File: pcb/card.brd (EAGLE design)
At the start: 69.5 x 40.6 mm, 19 parts, among them IC1 74HC14D, IC2 24LC256SN, Q1 BC817

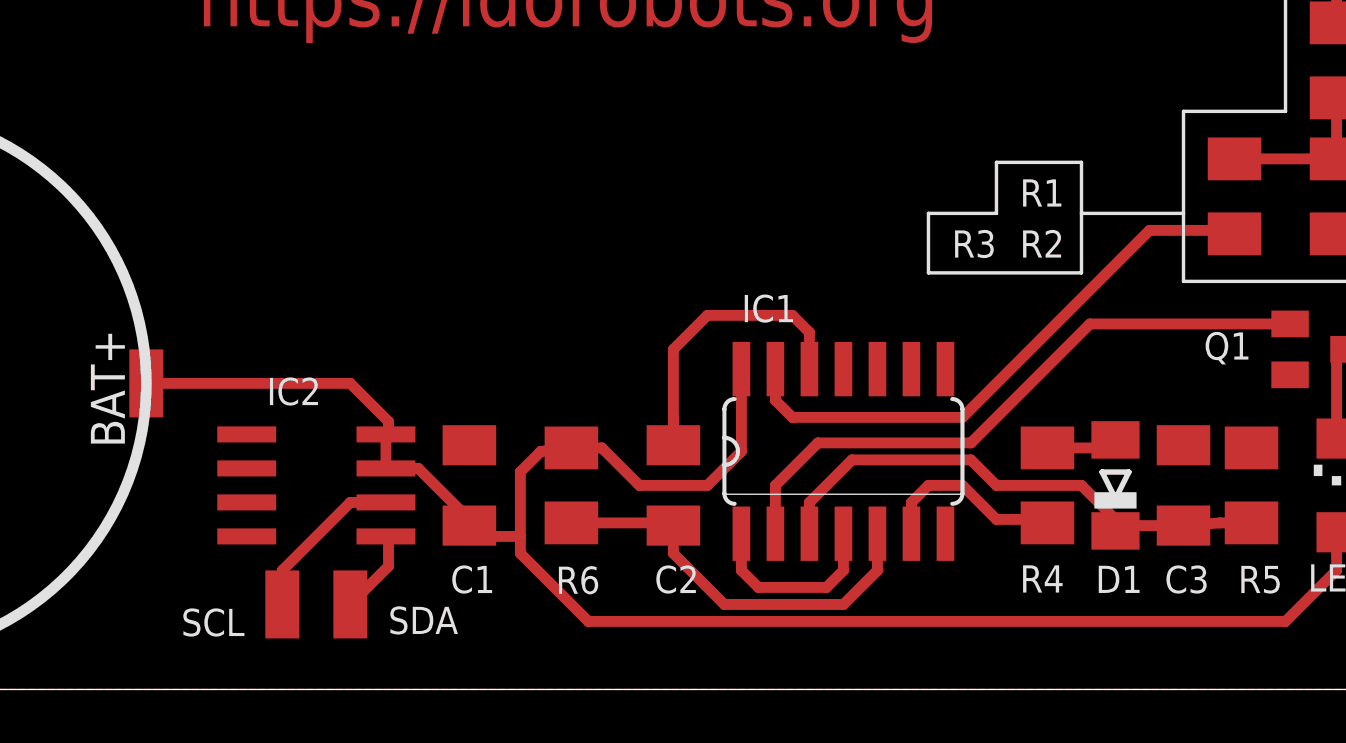
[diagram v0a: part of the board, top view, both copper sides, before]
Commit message: Added a GND pad for the EEPROM chip.
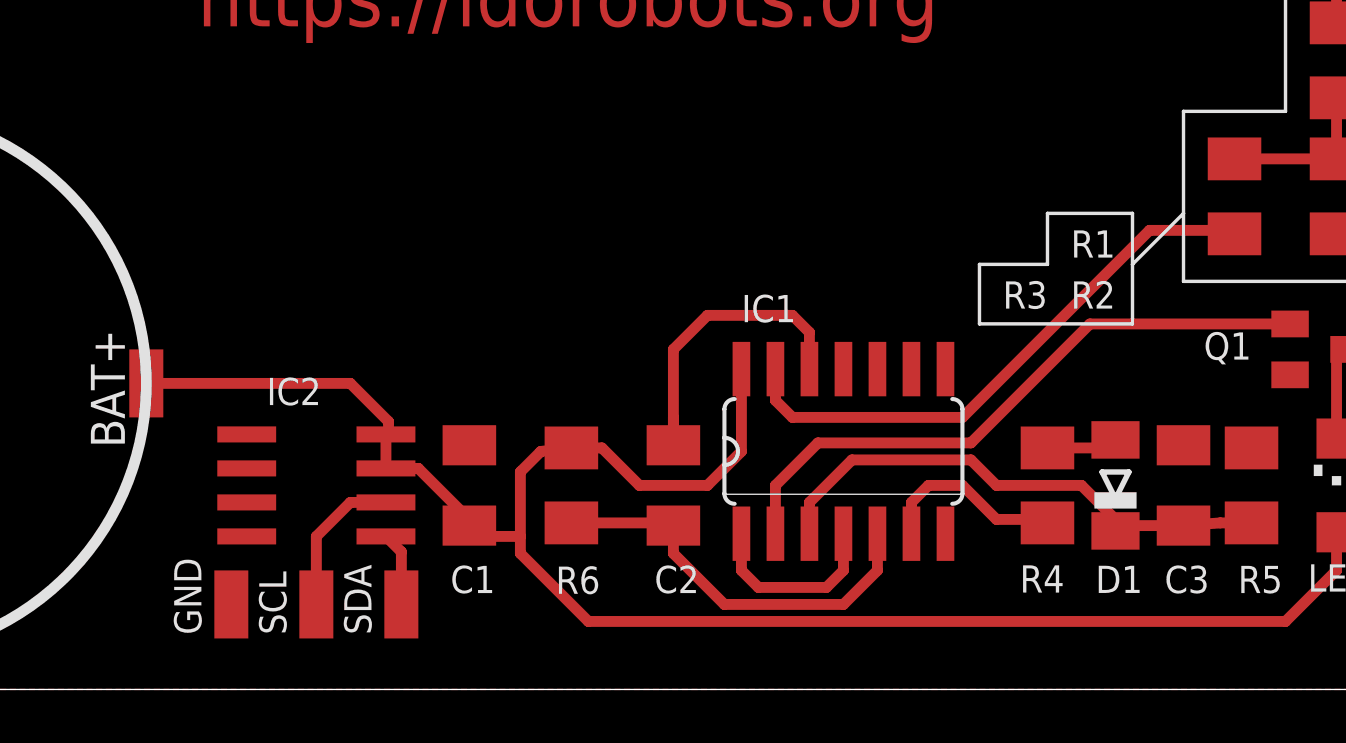
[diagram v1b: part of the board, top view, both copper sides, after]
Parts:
- added GND: (no value), wirepad:SMD1,27-2,54
- moved SDA 1.90 mm to (31.1, 3.17)
- moved SCL 1.27 mm to (27.9, 3.17)
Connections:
- net GND: now also GND.1
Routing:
- net N$9: track 6.19 -> 5.67 mm
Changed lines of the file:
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@@
 <setting verticaltext="up"/>
 </settings>
-<grid distance="0.635" unitdist="mm" unit="mm" style="lines" multiple="1" display="no" altdistance="0.003125" altunitdist="mic" altunit="mm"/>
+<grid distance="0.635" unitdist="mm" unit="mm" style="lines" multiple="1" display="no" altdistance="0.3175" altunitdist="mm" altunit="mm"/>
 <layers>
 <layer number="1" name="Top" color="4" fill="1" visible="yes" active="yes"/>
@@
 <text x="8.89" y="30.48" size="3.81" layer="29">Kajetan Rzepecki</text>
 <text x="23.495" y="24.765" size="2.1844" layer="29">https://idorobots.org</text>
-<wire x1="50.8" y1="15.5575" x2="56.515" y2="15.5575" width="0.127" layer="25"/>
-<wire x1="56.515" y1="15.5575" x2="56.515" y2="17.78" width="0.127" layer="25"/>
-<wire x1="56.515" y1="17.78" x2="56.515" y2="19.685" width="0.127" layer="25"/>
+<wire x1="52.705" y1="13.6525" x2="58.42" y2="13.6525" width="0.127" layer="25"/>
+<wire x1="58.42" y1="13.6525" x2="58.42" y2="15.875" width="0.127" layer="25"/>
+<wire x1="58.42" y1="15.875" x2="58.42" y2="17.78" width="0.127" layer="25"/>
 <wire x1="60.325" y1="15.24" x2="67.945" y2="15.24" width="0.127" layer="25"/>
 <wire x1="67.945" y1="15.24" x2="67.945" y2="26.67" width="0.127" layer="25"/>
 <wire x1="60.325" y1="17.78" x2="60.325" y2="15.24" width="0.127" layer="25"/>
-<wire x1="56.515" y1="17.78" x2="60.325" y2="17.78" width="0.127" layer="25"/>
-<wire x1="50.8" y1="15.5575" x2="50.8" y2="17.78" width="0.127" layer="25"/>
-<wire x1="50.8" y1="17.78" x2="53.34" y2="17.78" width="0.127" layer="25"/>
-<wire x1="53.34" y1="17.78" x2="53.34" y2="19.685" width="0.127" layer="25"/>
-<wire x1="56.515" y1="19.685" x2="53.34" y2="19.685" width="0.127" layer="25"/>
+<wire x1="58.42" y1="15.875" x2="60.325" y2="17.78" width="0.127" layer="25"/>
+<wire x1="52.705" y1="13.6525" x2="52.705" y2="15.875" width="0.127" layer="25"/>
+<wire x1="52.705" y1="15.875" x2="55.245" y2="15.875" width="0.127" layer="25"/>
+<wire x1="55.245" y1="15.875" x2="55.245" y2="17.78" width="0.127" layer="25"/>
+<wire x1="58.42" y1="17.78" x2="55.245" y2="17.78" width="0.127" layer="25"/>
 <wire x1="67.945" y1="26.67" x2="64.135" y2="26.67" width="0.127" layer="25"/>
 <wire x1="64.135" y1="26.67" x2="64.135" y2="21.59" width="0.127" layer="25"/>
@@
 </element>
 <element name="R1" library="resistor" package="M1206" value="1M" x="66.04" y="23.495" smashed="yes" rot="R90">
-<attribute name="NAME" x="55.88" y="19.05" size="1.016" layer="25" rot="R180"/>
+<attribute name="NAME" x="57.785" y="17.145" size="1.016" layer="25" rot="R180"/>
 </element>
 <element name="R2" library="resistor" package="M1206" value="20M" x="66.04" y="18.415" smashed="yes" rot="R90">
-<attribute name="NAME" x="55.88" y="17.145" size="1.016" layer="25" rot="R180"/>
+<attribute name="NAME" x="57.785" y="15.24" size="1.016" layer="25" rot="R180"/>
 </element>
 <element name="R3" library="resistor" package="M1206" value="1M" x="62.23" y="18.415" smashed="yes" rot="R90">
-<attribute name="NAME" x="53.34" y="17.145" size="1.016" layer="25" rot="R180"/>
+<attribute name="NAME" x="55.245" y="15.24" size="1.016" layer="25" rot="R180"/>
 </element>
 <element name="R4" library="resistor" package="M1206" value="200k" x="55.245" y="7.62" smashed="yes" rot="R270">
@@
 <attribute name="NAME" x="38.545009375" y="4.587546875" size="1.016" layer="25" rot="R180"/>
 </element>
-<element name="SDA" library="wirepad" package="SMD1,27-2,54" value="" x="29.21" y="3.175" smashed="yes">
-<attribute name="VALUE" x="29.21" y="3.175" size="0.0254" layer="27"/>
-<attribute name="NAME" x="30.62" y="2.07" size="1.016" layer="25"/>
-</element>
-<element name="SCL" library="wirepad" package="SMD1,27-2,54" value="" x="26.67" y="3.175" smashed="yes">
-<attribute name="VALUE" x="26.67" y="3.175" size="0.0254" layer="27"/>
-<attribute name="NAME" x="25.26" y="3.01" size="1.016" layer="25" rot="R180"/>
+<element name="SDA" library="wirepad" package="SMD1,27-2,54" value="" x="31.115" y="3.175" smashed="yes">
+<attribute name="VALUE" x="31.115" y="3.175" size="0.0254" layer="27"/>
+<attribute name="NAME" x="29.9975" y="2.045" size="1.016" layer="25" rot="R90"/>
+</element>
+<element name="SCL" library="wirepad" package="SMD1,27-2,54" value="" x="27.94" y="3.175" smashed="yes">
+<attribute name="VALUE" x="27.94" y="3.175" size="0.0254" layer="27"/>
+<attribute name="NAME" x="26.8225" y="2.045" size="1.016" layer="25" rot="R90"/>
 </element>
 <element name="BAT+" library="wirepad" package="SMD1,27-2,54" value="" x="21.59" y="11.43"/>
@@
 <attribute name="MPN" value="24LC256-I/SN" x="27.94" y="7.62" size="1.016" layer="27" rot="R270" display="off"/>
 <attribute name="NAME" x="26.082496875" y="10.619609375" size="1.016" layer="25"/>
+</element>
+<element name="GND" library="wirepad" package="SMD1,27-2,54" value="" x="24.765" y="3.175" smashed="yes">
+<attribute name="VALUE" x="24.765" y="3.175" size="0.0254" layer="27"/>
+<attribute name="NAME" x="23.6475" y="2.045" size="1.016" layer="25" rot="R90"/>
 </element>
 </elements>
@@
 <contactref element="Q1" pad="E"/>
 <contactref element="C1" pad="1"/>
-<polygon width="0.4064" layer="1" isolate="0.3048" orphans="yes">
+<polygon width="0.4064" layer="1" isolate="0.4064" orphans="yes">
 <vertex x="0" y="40.64"/>
 <vertex x="0" y="0"/>
@@
 <contactref element="IC2" pad="3"/>
 <contactref element="IC2" pad="4"/>
+<contactref element="GND" pad="1"/>
 </signal>
 <signal name="VCC">
@@
 <signal name="N$9">
 <contactref element="SCL" pad="1"/>
-<wire x1="29.21" y1="6.985" x2="26.67" y2="4.445" width="0.4064" layer="1"/>
-<wire x1="26.67" y1="4.445" x2="26.67" y2="3.175" width="0.4064" layer="1"/>
+<wire x1="29.21" y1="6.985" x2="27.94" y2="5.715" width="0.4064" layer="1"/>
+<wire x1="27.94" y1="5.715" x2="27.94" y2="3.175" width="0.4064" layer="1"/>
 <contactref element="IC2" pad="6"/>
 <wire x1="30.54" y1="6.985" x2="29.21" y2="6.985" width="0.4064" layer="1"/>
@@
 <signal name="N$10">
 <contactref element="SDA" pad="1"/>
-<wire x1="30.635" y1="4.6" x2="29.21" y2="3.175" width="0.4064" layer="1"/>
 <contactref element="IC2" pad="5"/>
-<wire x1="30.635" y1="4.6" x2="30.635" y2="5.62" width="0.4064" layer="1"/>
-<wire x1="30.635" y1="5.62" x2="30.54" y2="5.715" width="0.4064" layer="1"/>
+<wire x1="31.115" y1="3.175" x2="31.115" y2="5.14" width="0.4064" layer="1"/>
+<wire x1="31.115" y1="5.14" x2="30.54" y2="5.715" width="0.4064" layer="1"/>
 </signal>
 <signal name="ANT">

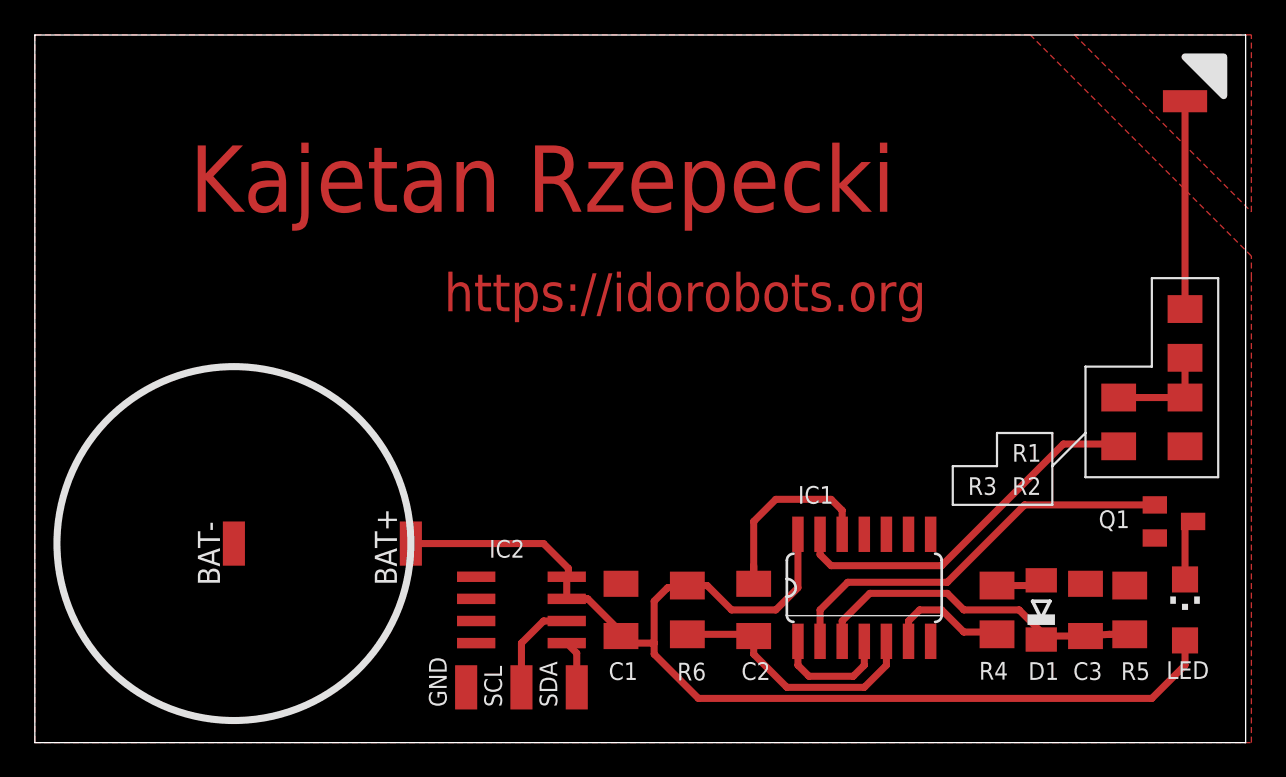
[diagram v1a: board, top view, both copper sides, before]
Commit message: Optimized the design.
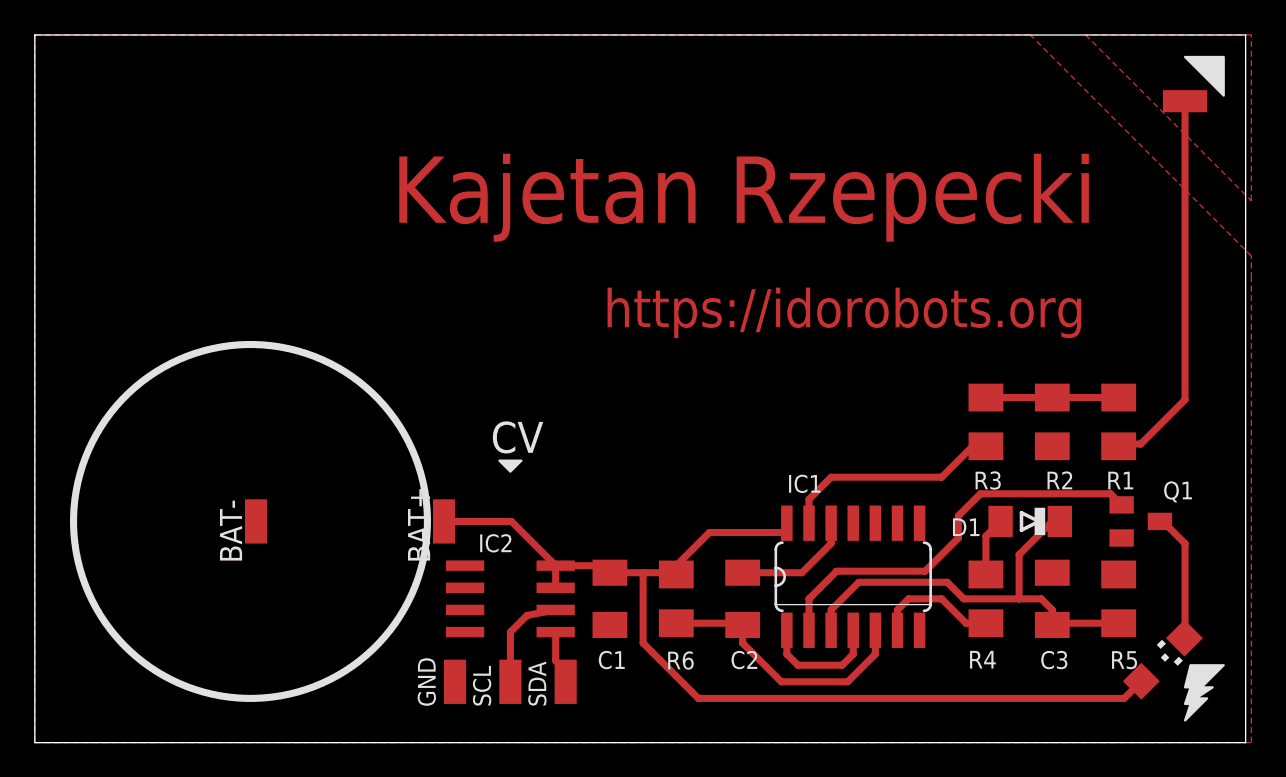
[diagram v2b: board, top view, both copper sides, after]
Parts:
- moved R2 7.62 mm to (58.4, 18.4)
- moved R3 7.62 mm to (54.6, 18.4)
- moved R1 6.35 mm to (62.2, 18.4), turned to 270 degrees
- moved D1 5.12 mm to (57.1, 12.7), turned to 180 degrees
- moved LED 3.13 mm to (64.8, 4.76), turned to 315 degrees
- moved BAT+ 2.29 mm to (23.5, 12.7)
- moved C3 2.01 mm to (58.4, 8.26)
- moved Q1 1.91 mm to (63.5, 12.7)
- moved BAT- 1.80 mm to (12.7, 12.7)
- moved R5 0.90 mm to (62.2, 8.26)
- moved R6 0.90 mm to (36.8, 8.26)
- moved IC2 0.90 mm to (27.3, 8.26)
- moved C1 0.90 mm to (33.0, 8.26), turned to 90 degrees
- moved C2 0.90 mm to (40.6, 8.26)
- moved R4 0.90 mm to (54.6, 8.26)
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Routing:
- net ANT: track 11.9 -> 23.0 mm
- net VCC: track 68.2 -> 58.9 mm
- net N$3: track 22.3 -> 13.5 mm
- net N$8: track 19.8 -> 25.6 mm
- net N$4: track 11.9 -> 6.94 mm
- net N$13: track 3.79 -> 7.41 mm
- net N$2: track 6.09 -> 7.62 mm
- net N$7: track 2.66 -> 3.39 mm
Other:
- board text added: "CV"

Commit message: Added a bypass cap & improved the layout.
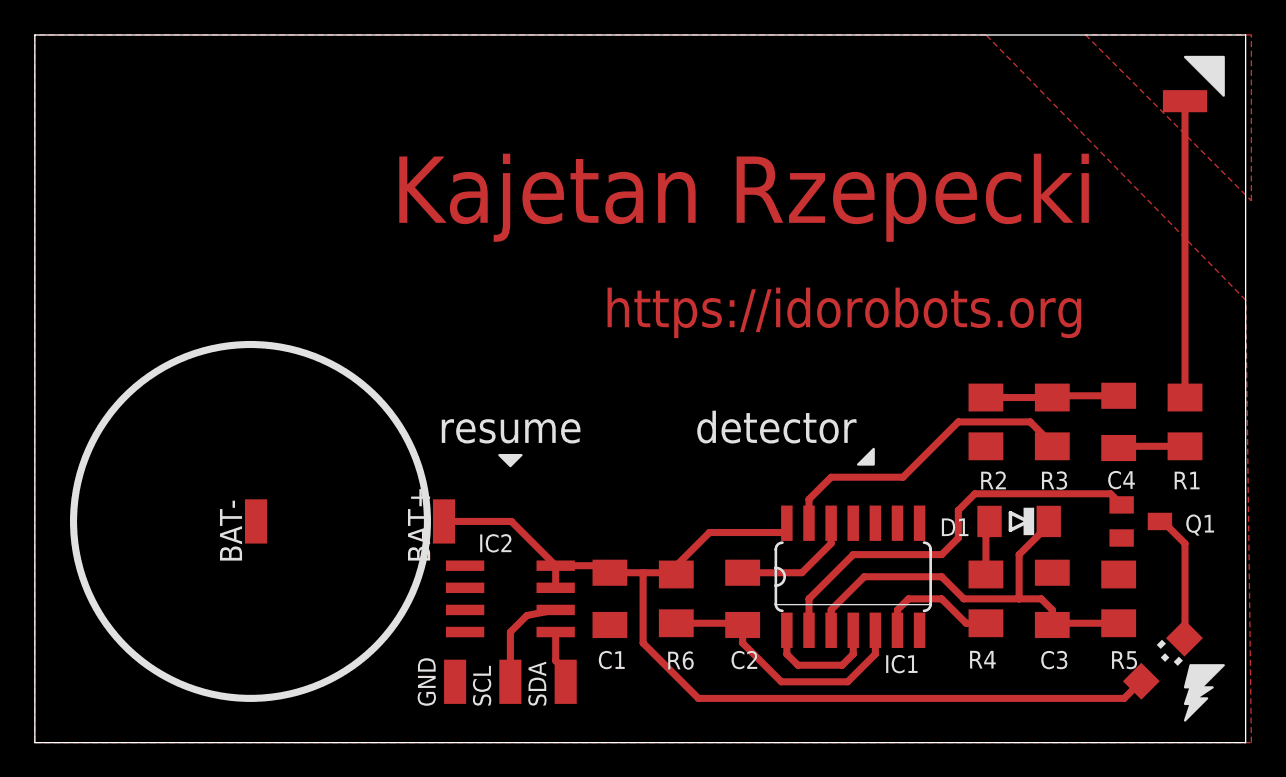
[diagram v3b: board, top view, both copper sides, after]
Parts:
- added C4: 10nF, resistor:C1206K
- R1, R3, R5, R6: value 1M -> 470k
- R2: value 20M -> 40M
- R4: value 200k -> 100k
- moved R1 3.81 mm to (66.0, 18.4), turned to 90 degrees
- moved R2 3.81 mm to (54.6, 18.4)
- moved R3 3.81 mm to (58.4, 18.4)
- moved D1 0.63 mm to (56.5, 12.7)
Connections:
- new net N$1: C4.1, R1.1
- net N$2: now also C4.2; no longer R1.1
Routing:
- net ANT: track 23.0 -> 17.7 mm
- net N$3: track 13.5 -> 18.8 mm
- net N$1: track 0.00 -> 4.46 mm
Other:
- board text added: "detector"
- board text added: "resume"
- board text removed: "CV"
